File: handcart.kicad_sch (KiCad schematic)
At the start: 26 parts, among them J1 Conn_01x05, J10 Conn_02x03_Odd_Even, J11 Conn_01x03, J12 Conn_01x04, J13 Conn_01x04, J132 TE_Ampseal_23, J14 Conn_01x03, J15 Conn_01x02, J16 Conn_01x02, J17 Conn_01x02, J18 Conn_01x02, J2 Conn_01x02, J23 Conn_02x05, J24 TE_AmpSeal_14_776273-1, J3 Conn_01x02, J4 Conn_01x02, J5 Conn_01x02, J6 Conn_01x02, J7 Conn_01x02, J8 Conn_01x02, J9 Conn_01x02, U1 Tex_DCDC_v2, U2 DCDC2510

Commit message: Major changes after the schematic review. Refer to Github for all the changes
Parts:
- removed J12, J13: Conn_01x04, Connector_Molex:Molex_Micro-Fit_3.0_43650-0400_1x04_P3.00mm_Horizontal, symbol Connector_Generic:Conn_01x04
- removed J15, J16, J17: Conn_01x02, Connector_Molex:Molex_Micro-Fit_3.0_43650-0215_1x02_P3.00mm_Vertical, symbol Connector_Generic:Conn_01x02
- removed J18: Conn_01x02, Connector_Molex:Molex_Micro-Fit_3.0_43650-0200_1x02_P3.00mm_Horizontal, symbol Connector_Generic:Conn_01x02
- added D1: 1N4148W, Diode_SMD:D_SOD-323_HandSoldering, symbol Device:D_Small
- added D?: 5V, symbol Device:LED
- added D?: 12V, symbol Device:LED
- added D?: 24V, symbol Device:LED
- added D?: VSD, symbol Device:LED
- added D?: 3V3, symbol Device:LED
- added F1: 20A, Eagle_Main:Keystone-Fuseholder 3557-2, symbol Device:Fuse
- added F2: 15A, Eagle_Main:Keystone-Fuseholder 3557-2, symbol Device:Fuse
- added F3: 1A, Eagle_Main:Keystone-Fuseholder 3557-2, symbol Device:Fuse
- added J10: SPARE_SUPPLY, symbol Connector_Generic:Conn_02x03_Odd_Even
- added J14: ADD_FAN, Connector_Molex:Molex_Micro-Fit_3.0_43650-0215_1x02_P3.00mm_Vertical, symbol Connector_Generic:Conn_01x02
- added Q1: SSM3K361TU,LF, 00_proj-lib:SOTFL65P210X75-3N, symbol Device:Q_NMOS_GSD
- added R1: 22R, Resistor_SMD:R_0603_1608Metric, symbol Device:R
- added R2: 330k, Resistor_SMD:R_0603_1608Metric, symbol Device:R
- added R? (x2): 1k, symbol Device:R
- added R?: 330R, symbol Device:R
- added R?: 2k2, symbol Device:R
- added R?: 270R, symbol Device:R
- added TP?: TP_24V, symbol Connector:TestPoint
- added TP?: TP_3V3, symbol Connector:TestPoint
- added TP?: TP_12V, symbol Connector:TestPoint
- added TP?: TP_5V, symbol Connector:TestPoint
- added TP?: TP_VSD, symbol Connector:TestPoint
- J1: value Conn_01x05 -> ROTARY ENCODER
- J12: renamed from J10; value Conn_02x03_Odd_Even -> SPARE_CHARGER
- J13: renamed from J23; value Conn_02x05 -> SPARE_BMS
- J15: renamed from J14; value Conn_01x03 -> EXT_SCREEN
- J16: renamed from J24; value TE_AmpSeal_14_776273-1 -> CHARGER
- J17: renamed from J132; value TE_Ampseal_23 -> BMS
- J2: value Conn_01x02 -> ARROW_KEYS_1
- J3: value Conn_01x02 -> ARROW_KEYS_2
- J4: value Conn_01x02 -> ARROW_KEYS_3
- J5: value Conn_01x02 -> ARROW_KEYS_4
- J6: value Conn_01x02 -> RESET_BUTTON
- J7: value Conn_01x02 -> TSMS
- J8: value Conn_01x02 -> MUSHROOM
- JP1: value SolderJumper_2_Open -> RASPBERRY_bypass
- RN1, RN2: footprint Resistor_SMD:R_Array_Convex_4x0612 -> Resistor_SMD:R_Array_Convex_4x0603
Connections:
- net +12V: now also F2.2, J10.3 (Pin_3), R?.1, TP?.1; no longer J16.13, J17.1, U2.11 (VDD), U2.12 (VDD), U2.13 (VDD), U2.14 (VDD)
- net +24V: now also J17.1, D1.1 (K), F1.2, J10.1 (Pin_1), J14.1 (Pin_1), R?.1, TP?.1; no longer J16.11, J8.1 (Pin_1), J9.1 (Pin_1)
- net +3V3: now also J10.4 (Pin_4), R?.1, TP?.1
- net +5V: now also J10.2 (Pin_2), R?.1, TP?.1
- net GND: now also D?.1 (K), D?.1 (K), D?.1 (K), D?.1 (K), D?.1 (K), J10.5 (Pin_5), J10.6 (Pin_6), Q1.2 (S), R2.2; no longer J16.12
- net SD_FROM_MUSHROOM: no longer J8.2 (Pin_2)
- net SD_TO_CHARGER: now also J8.2 (Pin_2)
- net NC_CRG_4: now reaches J12.4 (Pin_4)
- net NC_CRG_4: now also J16.11
- net NC_CRG_5: now reaches J12.5 (Pin_5)
- net NC_CRG_5: now also J16.12
- net NC_CRG_6: now reaches J12.6 (Pin_6)
- net NC_CRG_6: now also J16.13
- new net: F2.1, F3.1, U2.11 (VDD), U2.12 (VDD), U2.13 (VDD), U2.14 (VDD)
- new net: Q1.1 (G), R1.1, R2.1
- new net: D1.2 (A), J14.2 (Pin_2), Q1.3 (D)
- new net: D?.2 (A), R?.2 (x5)
- new net: F1.1, J9.1 (Pin_1)
- new net ADD_FAN_PWM: R1.2
- new net SD_TO_MUSHROOM: J8.1 (Pin_1)
- new net VCC: F3.2, R?.1, TP?.1
- no-connect marks 5 -> 2
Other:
- sheet Shutdown renamed Shutdown+Discharge
- removed sheet Discharge
- sheet Output ports: added none; removed GREEN_TS_OFF, RED_BMS_FAULT, RED_IMD_FAULT, STRIP1_B, STRIP1_G, STRIP1_R, TSAL_B, TSAL_G, TSAL_R
- sheet Shutdown+Discharge: file Shutdown.kicad_sch -> Shutdown_Discharge.kicad_sch
- sheet Shutdown+Discharge ports: added PON_DISCHARGE, SD_TO_MUSHROOM; removed SD_FROM_MUSHROOM, SD_TO_CHARGER
- note added: "-->----------------\ <--SD_FROM_CHARGER /"
- note added: "/------------> \-MUSHROOM<---"
- note added: "ADDITIONAL 24V DC PWM FAN"
- note added: "EXTERNAL SCREEN OF THE RASPBERRY"
- note added: "EXTERNAL SCREEN POWER SUPPLY"
- note added: "For the resistors value: Id = 0.01A , Vd = 2V"
- note added: "Used to bypass the relay"
- note removed: "ARROW_KEYS"
- note removed: "BMS FAULT INDICATORS"
- note removed: "DIRECT TO THE BMS MAIN BOARD"
- note removed: "EXTERNAL DISCHARGE RELAY"
- note removed: "EXTERNAL MONITOR OF THE RASPBERRY 5V and 3V3 for the screen's shield -->"
- note removed: "EXTERNAL RGB STRIP"
- note removed: "MOLEX OUTPUTs"
- note removed: "MUSHROOM ON PANEL"
- note removed: "RASPBERRY BYPASS just in case we need to remove the relay"
- note removed: "ROTARY ENCODER"
- note removed: "SD START"
- note removed: "Shouldn't change between the SD_BMS_OUT and the SD_END_HV because until the last one is closed there is no supply voltage on the line"
- note removed: "TSAL OUTPUT"
- note removed: "TSMS"
- note removed: "____________ V SD_FROM_CHARGER =>"
- moved on the sheet: J1, J11, J12, J13, J15, J16A, J16B, J16C, J2, J3, J4, J5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

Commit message: modified schematic and started design pcb
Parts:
- removed J11: Conn_01x03, Connector_Molex:Molex_Micro-Fit_3.0_43650-0300_1x03_P3.00mm_Horizontal, symbol Connector_Generic:Conn_01x03
- added D11, D12, D13, D14, D15: BAT54S, Package_TO_SOT_SMD:SOT-23, symbol Diode:BAT54S
- added D16: DDZ13ASF 13V, Diode_SMD:D_SOD-323F, symbol Device:D_Zener
- D10, D4, D6, D8, D9: renamed from D?; footprint (none) -> Resistor_SMD:R_0805_2012Metric
- F1: value 20A -> 10A
- F2: value 15A -> 5A
- F3: value 1A -> 2A
- J10: footprint (none) -> Connector_Molex:Molex_Micro-Fit_3.0_43045-0612_2x03_P3.00mm_Vertical
- J9: value Conn_01x02 -> POWER_IN
- R46, R47, R48, R49, R50: renamed from R?; footprint (none) -> Resistor_SMD:R_0603_1608Metric
- TP1, TP2, TP3, TP4, TP5: renamed from TP?; footprint (none) -> TestPoint:TestPoint_Pad_D2.0mm
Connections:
- net SD_END_HV is gone; now on net SD_END: J17.18
- net +5V: now also D12.2, D13.2, D14.2, D15.2
- net BMS_LED: now also D15.3
- net GND: now also D11.1, D12.1, D13.1, D14.1, D15.1, D16.2 (A)
- net IMD_LED: now also D14.3
- net PON: now also D13.3
- net SD_END: now also D16.1 (K)
- net TSAL: now also D12.3
- net at F1.1, J9.1 (Pin_1): now also D11.3
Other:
- sheet RS_232 renamed RS_232+FEEDBACK
- sheet RS_232+FEEDBACK: file RS_232.kicad_sch -> RS_232_FEEDBACK.kicad_sch
- sheet RS_232+FEEDBACK ports: added 12V_FB, COIL_DISCHARGE_FB, DIN, DOUT, PON_FB, RELE_SUTHDOWN_FB, SCLK, SD_BMS_IN_FB, SD_BMS_OUT_FB, SD_END_FB, SD_TO_CHARGER_FB, SD_TO_MUSHROOM_FB, VSD_FB, ~{CS}; removed none
- sheet Raspberry ports: added RASP_CLK, RASP_MISO, RASP_MOSI, RASP_~{CS}; removed CAN_N, CAN_P
- sheet Shutdown+Discharge ports: added COIL_DISCHARGE_FB, RELE_SHUTDOWN_FB; removed SD_END_HV
- note added: "-->-------\ <---SD_BMS /"
- note added: "/------------> \-----TSMS<---"
- note added: ":IMD_CHASSIS"
- note added: "SD_END--> TO_AIR"
- note removed: "CAN DIRECT CONNECTION"
- note removed: "IMD_CHASSIS:"
- moved on the sheet: D10, D4, D6, D8, D9, F1, F2, F3, J1, J10, J2, J3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

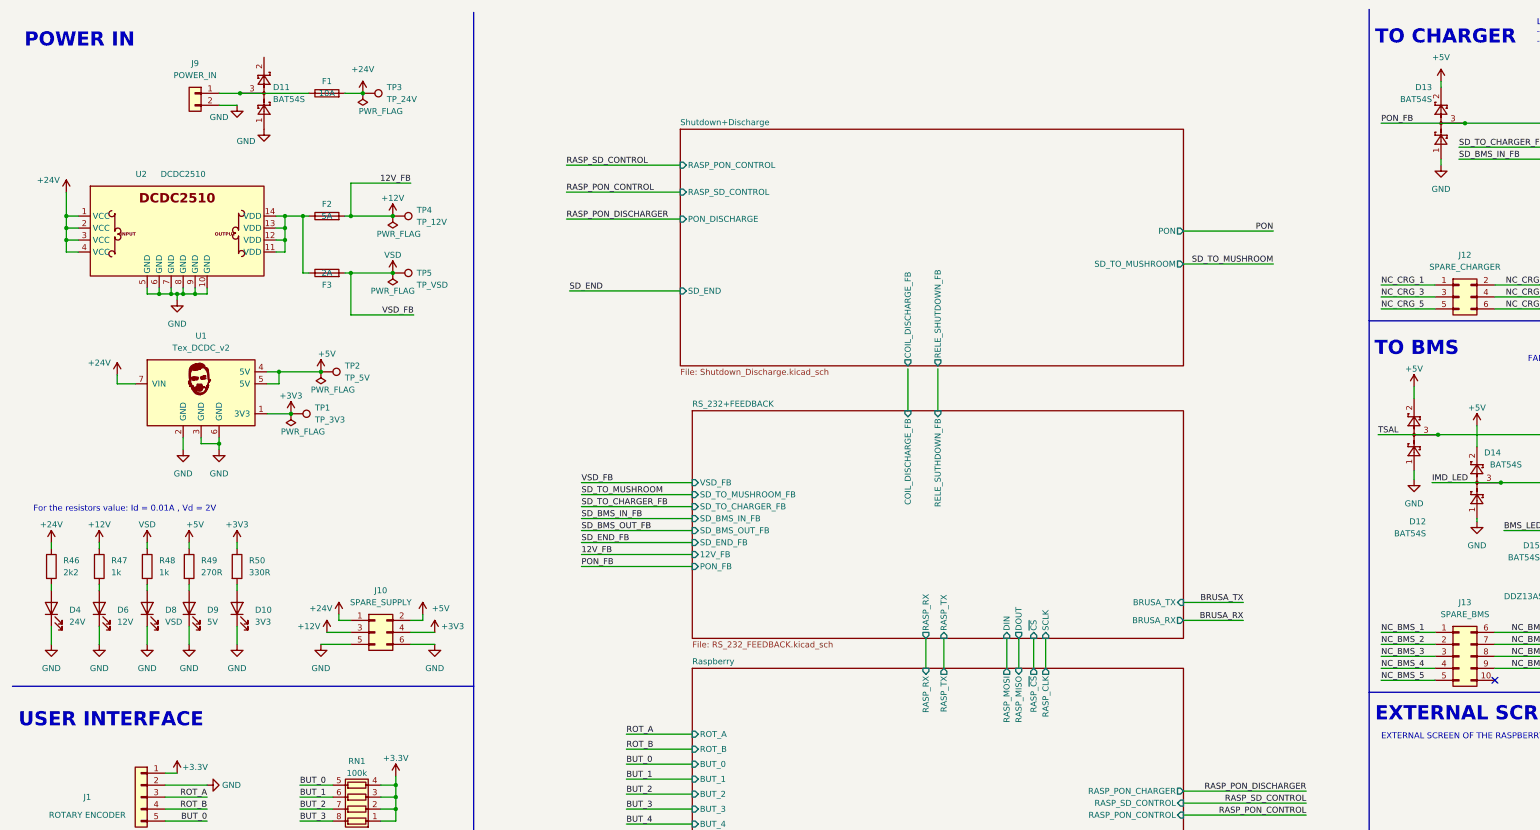
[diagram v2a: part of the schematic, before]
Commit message: Fixed frequency of LPF, added reverse polarity protection
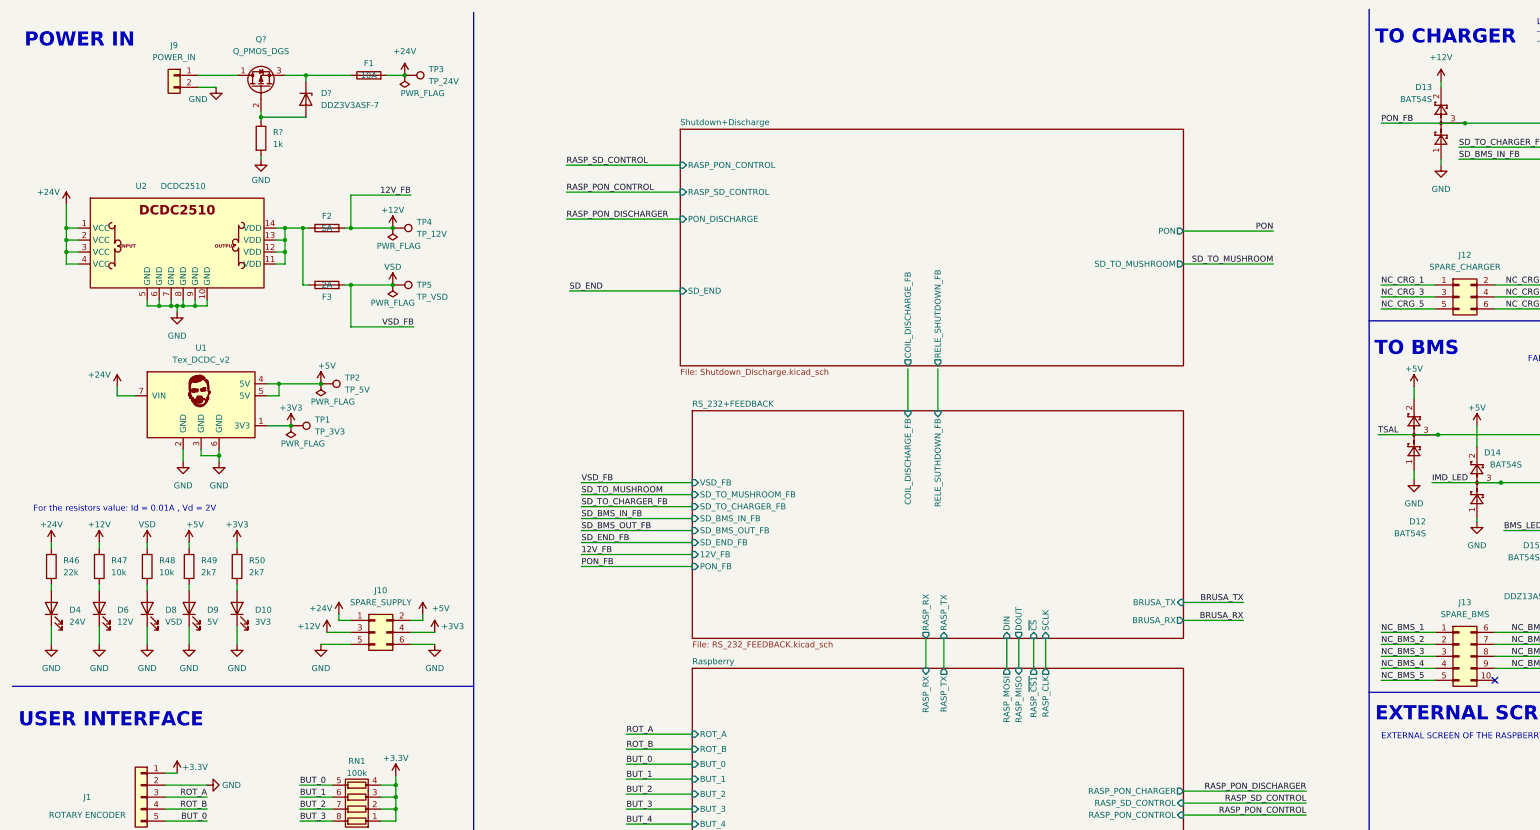
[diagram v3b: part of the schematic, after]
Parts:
- removed D11: BAT54S, Package_TO_SOT_SMD:SOT-23, symbol Diode:BAT54S
- added D?: DDZ3V3ASF-7, Diode_SMD:D_SOD-323, symbol Device:D_Zener
- added Q?: Q_PMOS_DGS, symbol Device:Q_PMOS_DGS
- added R?: 1k, symbol Device:R
- R46: value 2k2 -> 22k
- R47, R48: value 1k -> 10k
- R49: value 270R -> 2k7
- R50: value 330R -> 2k7
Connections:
- net +12V: now also D13.2
- net +5V: no longer D13.2
- net GND: now also R?.2
- net at F1.1: now also D?.1 (K), Q?.3 (S); no longer J9.1 (Pin_1)
- new net: D?.2 (A), Q?.2 (G), R?.1
- new net: J9.1 (Pin_1), Q?.1 (D)
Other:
- sheet Raspberry ports: added RASP_~{CS1}; removed RASP_~{CS}
- moved on the sheet: F1, F2, F3, J9, TP1, TP2, TP3, TP4, TP5, U1, U2

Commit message: First version of the pcb layout
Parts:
- J17: footprint Eagle_Connectors:TE_1-776228-4 -> Eagle_Connectors:TE_776087-4
- Q17: renamed from Q?; value Q_PMOS_DGS -> FQP17P06; footprint (none) -> Package_TO_SOT_THT:TO-220-3_Vertical
- R71: renamed from R?; footprint (none) -> Resistor_SMD:R_0603_1608Metric
- gave numbers to parts that had none: 1
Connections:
- net SD_FROM_MUSHROOM is gone; now on net VCC: JP1.1 (A)
- net BUT_0: now also RN2.7 (R2.2); no longer RN1.5 (R4.2)
- net BUT_1: now also RN1.8 (R1.2); no longer RN1.6 (R3.2)
- net BUT_3: now also RN1.6 (R3.2); no longer RN1.8 (R1.2)
- net BUT_4: now also RN1.5 (R4.2); no longer RN2.5 (R4.2)
- net ROT_A: now also RN2.5 (R4.2); no longer RN2.6 (R3.2)
- net ROT_B: now also RN2.6 (R3.2); no longer RN2.7 (R2.2)
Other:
- sheet Output ports: added ADD_RGB_STRIP; removed ADD_FAN_PWM
- sheet Raspberry ports: added ADD_RGB_STRIP; removed none
